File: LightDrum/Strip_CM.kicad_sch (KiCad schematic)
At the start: 42 parts, among them T1 NET-TIE, T10 NET-TIE, T11 NET-TIE, T12 NET-TIE, T13 NET-TIE, T14 NET-TIE, T15 NET-TIE, T16 NET-TIE, T2 NET-TIE, T3 NET-TIE, T4 NET-TIE, T5 NET-TIE, T6 NET-TIE, T7 NET-TIE, T8 NET-TIE, T9 NET-TIE, U5 INA4181 A2, U6 INA4181 A2

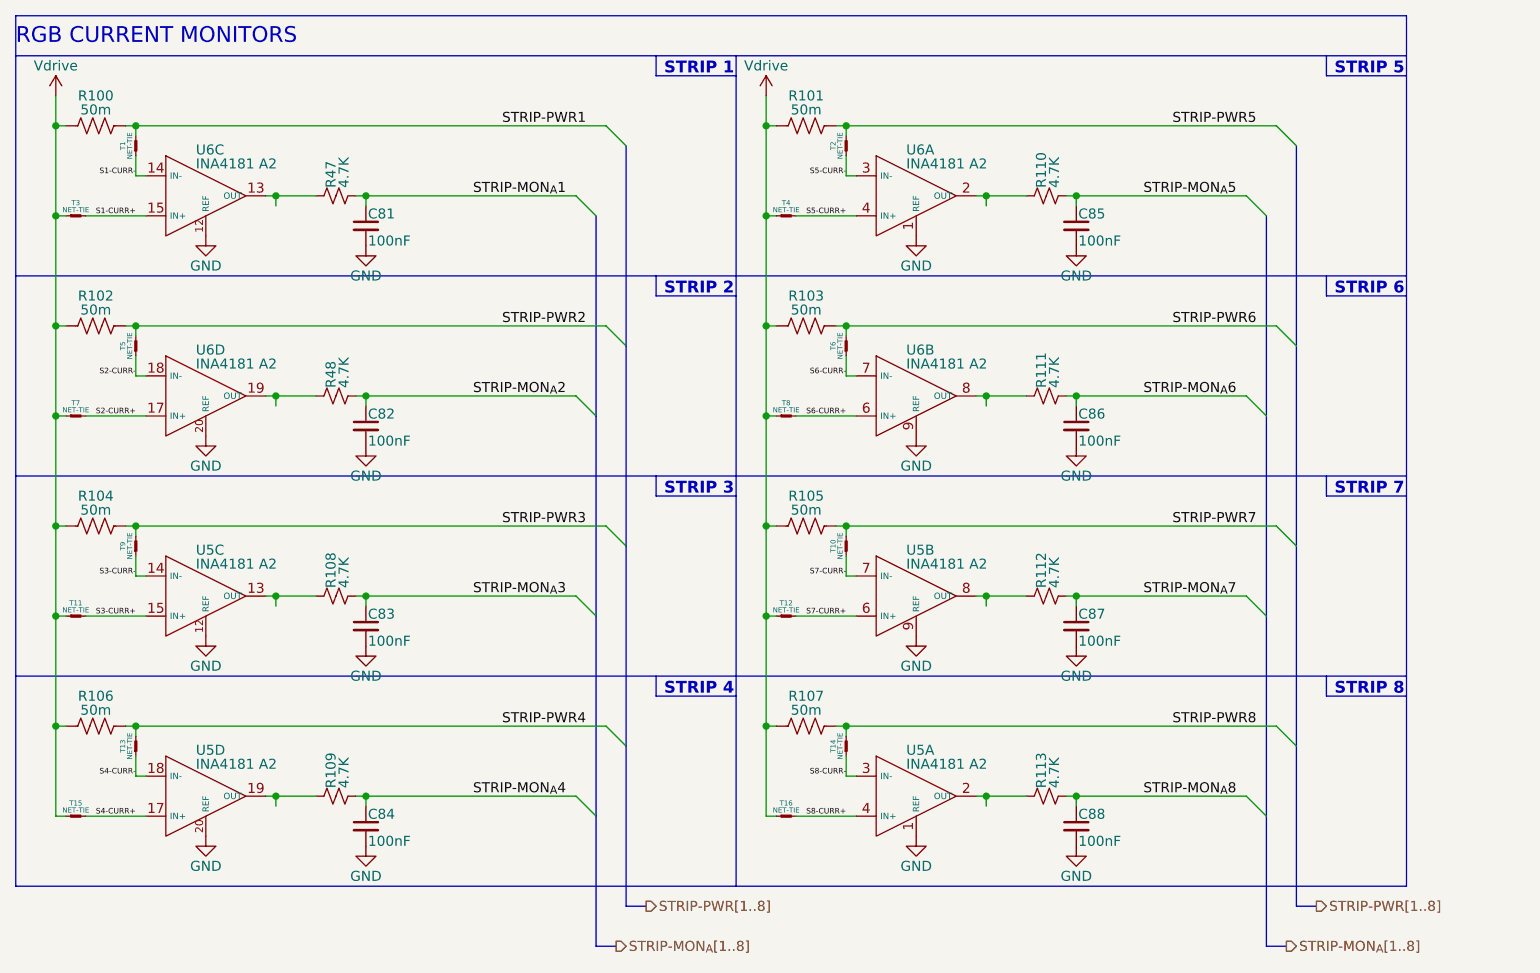
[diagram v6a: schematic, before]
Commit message: Organize old files and generate interface gerbers
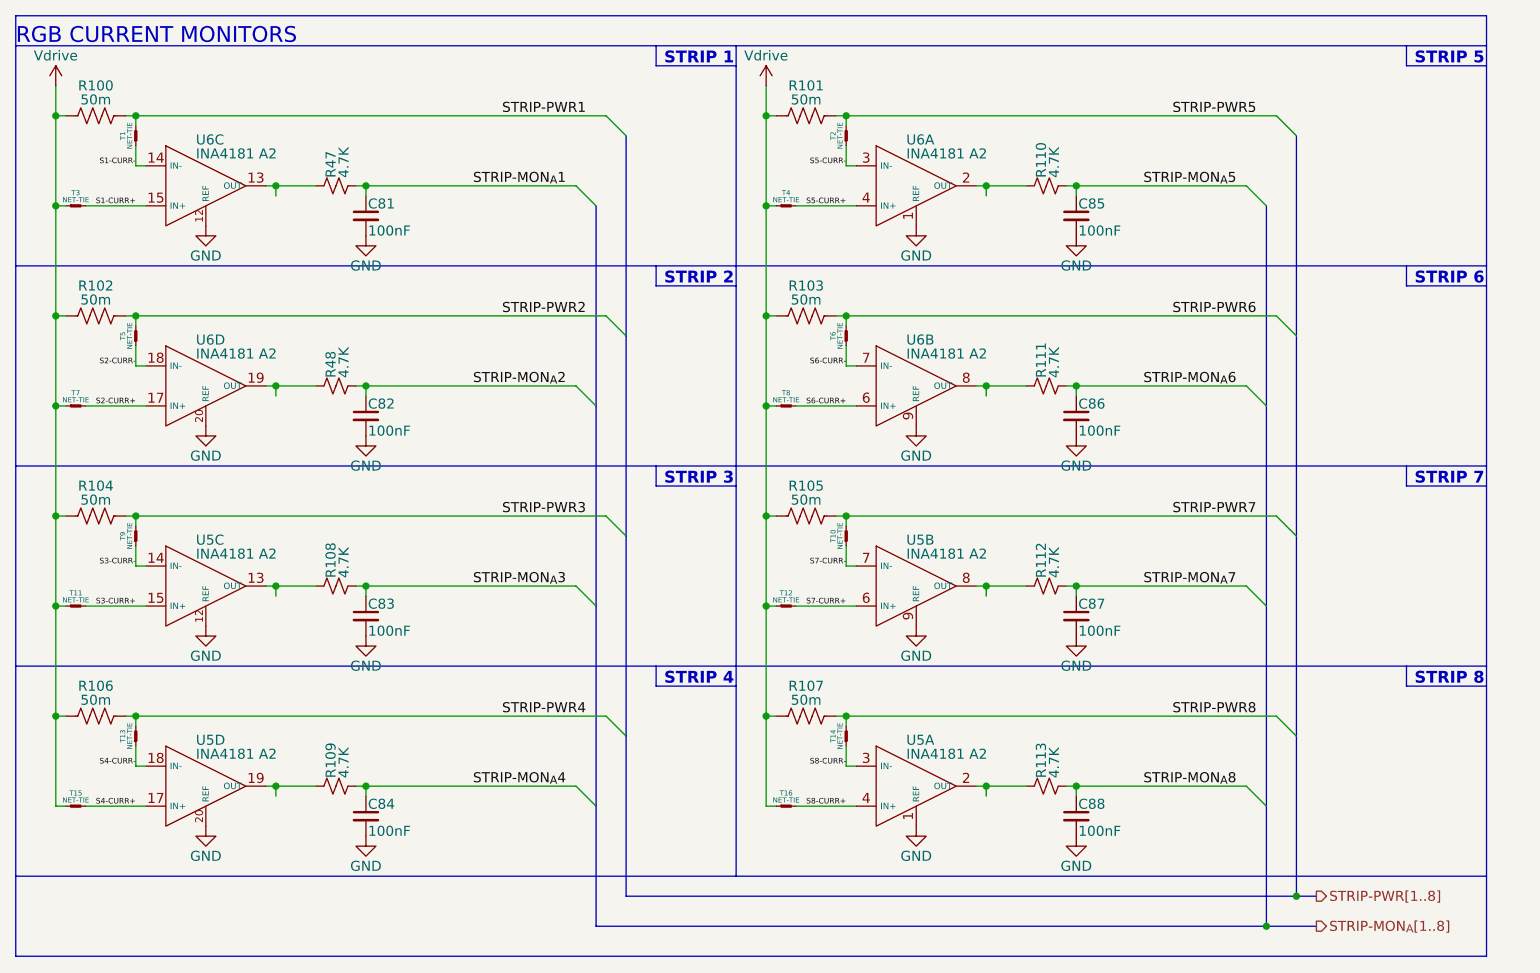
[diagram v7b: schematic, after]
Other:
- moved on the sheet: C81, C82, C83, C84, C85, C86, C87, C88, R100, R101, R102, R103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
